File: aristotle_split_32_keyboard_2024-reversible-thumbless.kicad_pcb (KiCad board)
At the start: 2 copper layers, 100 x 87.7 mm, 43 parts, among them J1 8P8C, J2 Screw_Terminal_01x04, J3 Screw_Terminal_01x04, K13 SW_SPDT, K14 SW_SPDT, K15 SW_SPDT, K16 SW_SPDT, K17 SW_SPDT, K23 SW_SPDT, K24 SW_SPDT, K25 SW_SPDT, K26 SW_SPDT, K27 SW_SPDT, K4 SW_SPDT, K5 SW_SPDT, K6 SW_SPDT, K7 SW_SPDT, SW1 SW_SPDT, U1 ProMicro_r

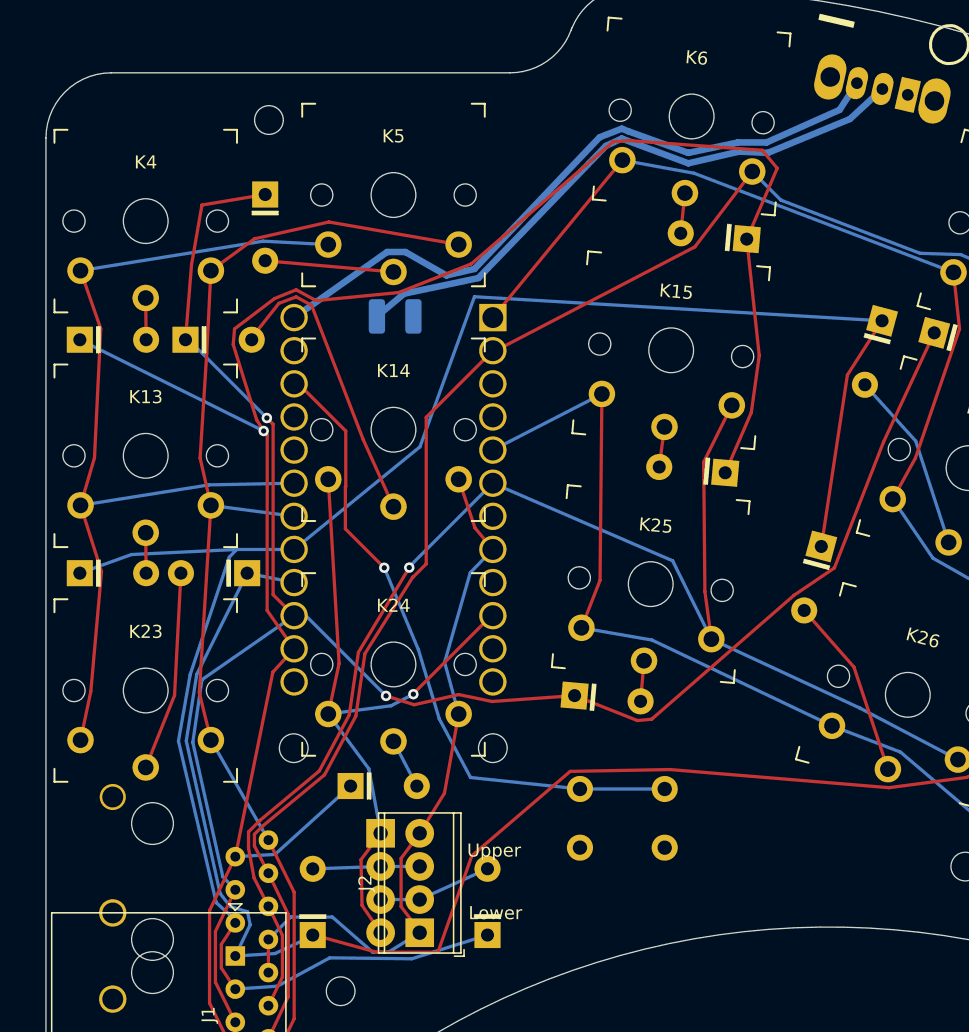
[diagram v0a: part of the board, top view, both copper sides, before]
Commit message: Move MCU up; reroute all wires to it; adjust screw positions
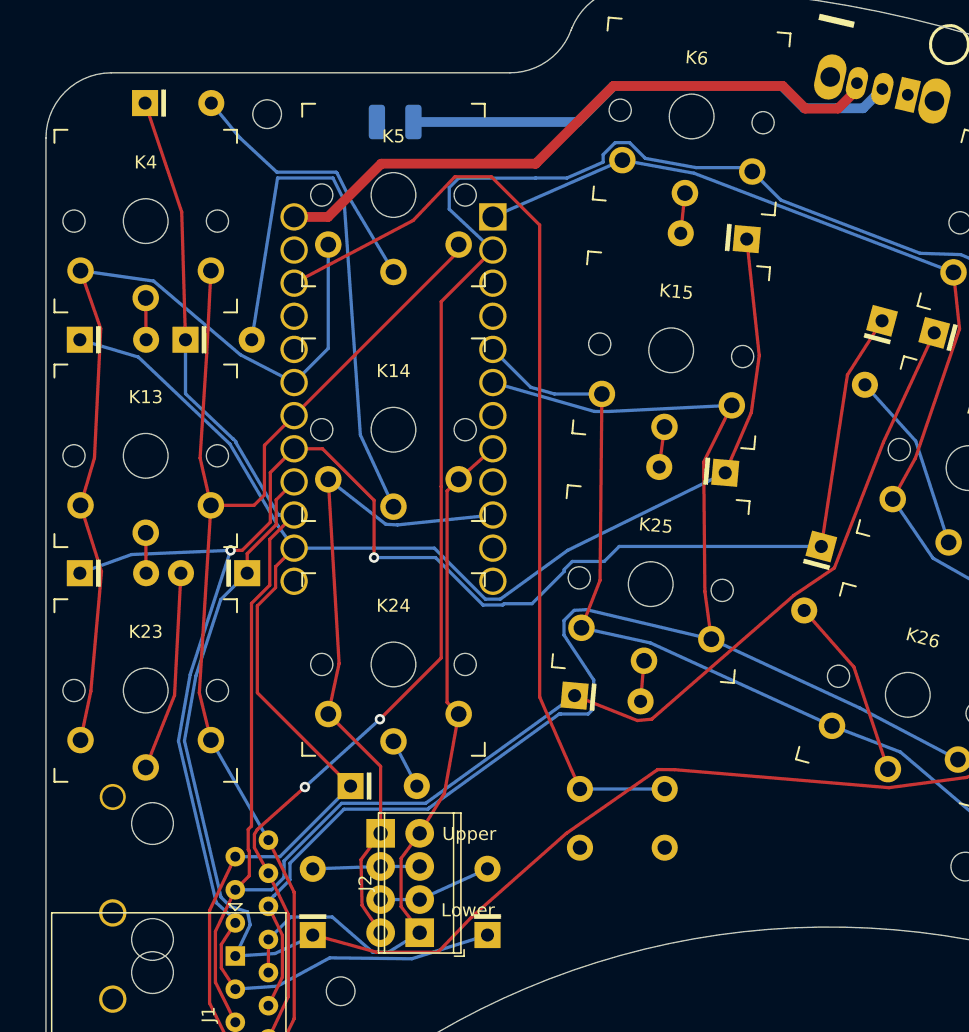
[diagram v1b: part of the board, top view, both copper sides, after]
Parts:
- removed H3: MountingHole, MountingHole:MountingHole_2.2mm_M2
- removed the H4 at (100.0, 130.4)
- moved BT1 14.9 mm to (107.8, 82.4), turned to 180 degrees
- moved D5 11.6 mm to (88.6, 81.0), turned to 0 degrees
- moved U1 7.72 mm to (107.7, 103.7)
- moved H4 0.47 mm to (98.0, 81.8)
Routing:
- net row0: track 157.0 -> 129.1 mm, vias 1 -> 0
- net Net-(U1-RST): track 49.2 -> 73.4 mm, vias 1 -> 0
- net Net-(D14-A): track 22.8 -> 42.8 mm
- net col1: track 153.7 -> 169.7 mm, vias 0 -> 2
- net Net-(D5-A): track 9.88 -> 20.7 mm
- net row1: track 143.9 -> 153.6 mm, vias 2 -> 0
- net col2: track 129.4 -> 137.6 mm, vias 1 -> 0
- net VCC: track 45.8 -> 38.4 mm
- net col7: track 72.5 -> 67.5 mm
- net col6: track 84.2 -> 79.4 mm
- net col0: track 90.3 -> 93.6 mm
- net Net-(SW1-C): track 51.8 -> 49.1 mm
- net row3: track 121.9 -> 124.6 mm
- net col3: track 54.4 -> 56.9 mm
- net row2: track 147.1 -> 146.1 mm, vias 0 -> 2
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
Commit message: Fix mounting holes
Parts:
- U1: value ProMicro_r -> Nice Nano
- renumbered H4 to H1, H4 to H2, H4 to H3
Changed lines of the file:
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@@
     (property "ki_keywords" "mounting hole")
     (attr exclude_from_pos_files)
-    (fp_text reference "H4" (at 0 -3.2) (layer "F.SilkS") hide
+    (fp_text reference "H1" (at 0 -3.2) (layer "F.SilkS") hide
         (effects (font (size 1 1) (thickness 0.15)))
     )
@@
     (property "ki_keywords" "mounting hole")
     (attr exclude_from_pos_files)
-    (fp_text reference "H4" (at 0 -3.2) (layer "F.SilkS") hide
+    (fp_text reference "H2" (at 0 -3.2) (layer "F.SilkS") hide
         (effects (font (size 1 1) (thickness 0.15)))
     )
@@
     (property "ki_keywords" "mounting hole")
     (attr exclude_from_pos_files)
-    (fp_text reference "H4" (at 0 -3.2) (layer "F.SilkS") hide
+    (fp_text reference "H3" (at 0 -3.2) (layer "F.SilkS") hide
         (effects (font (size 1 1) (thickness 0.15)))
     )
@@
         (effects (font (size 1 1) (thickness 0.15)) (justify mirror))
     )
-    (fp_text value "ProMicro_r" (at 4.07 -0.03 180) (layer "B.SilkS")
+    (fp_text value "Nice Nano" (at 5.15 -0.03 180) (layer "B.SilkS")
         (effects (font (size 1 1) (thickness 0.15)) (justify mirror))
     )
@@
     (stroke (width 0.12) (type default)) (layer "F.SilkS"))
   (gr_circle (center 97 121.5) (end 99.45 121.5)
-    (stroke (width 0.1) (type default)) (fill none) (layer "Eco1.User"))
+    (stroke (width 0.1) (type default)) (fill none) (layer "Dwgs.User"))
   (gr_circle (center 118.8 86.8) (end 121.25 86.8)
-    (stroke (width 0.1) (type default)) (fill none) (layer "Eco1.User"))
+    (stroke (width 0.1) (type default)) (fill none) (layer "Dwgs.User"))
   (gr_circle (center 96.5 86.8) (end 98.95 86.8)
-    (stroke (width 0.1) (type default)) (fill none) (layer "Eco1.User"))
+    (stroke (width 0.1) (type default)) (fill none) (layer "Dwgs.User"))
   (gr_circle (center 118.3 121.5) (end 120.75 121.5)
-    (stroke (width 0.1) (type default)) (fill none) (layer "Eco1.User"))
+    (stroke (width 0.1) (type default)) (fill none) (layer "Dwgs.User"))
   (gr_arc (start 179.010876 88.986461) (mid 180.348789 90.471737) (end 181 92.361706)
     (stroke (width 0.05) (type solid)) (layer "Edge.Cuts"))

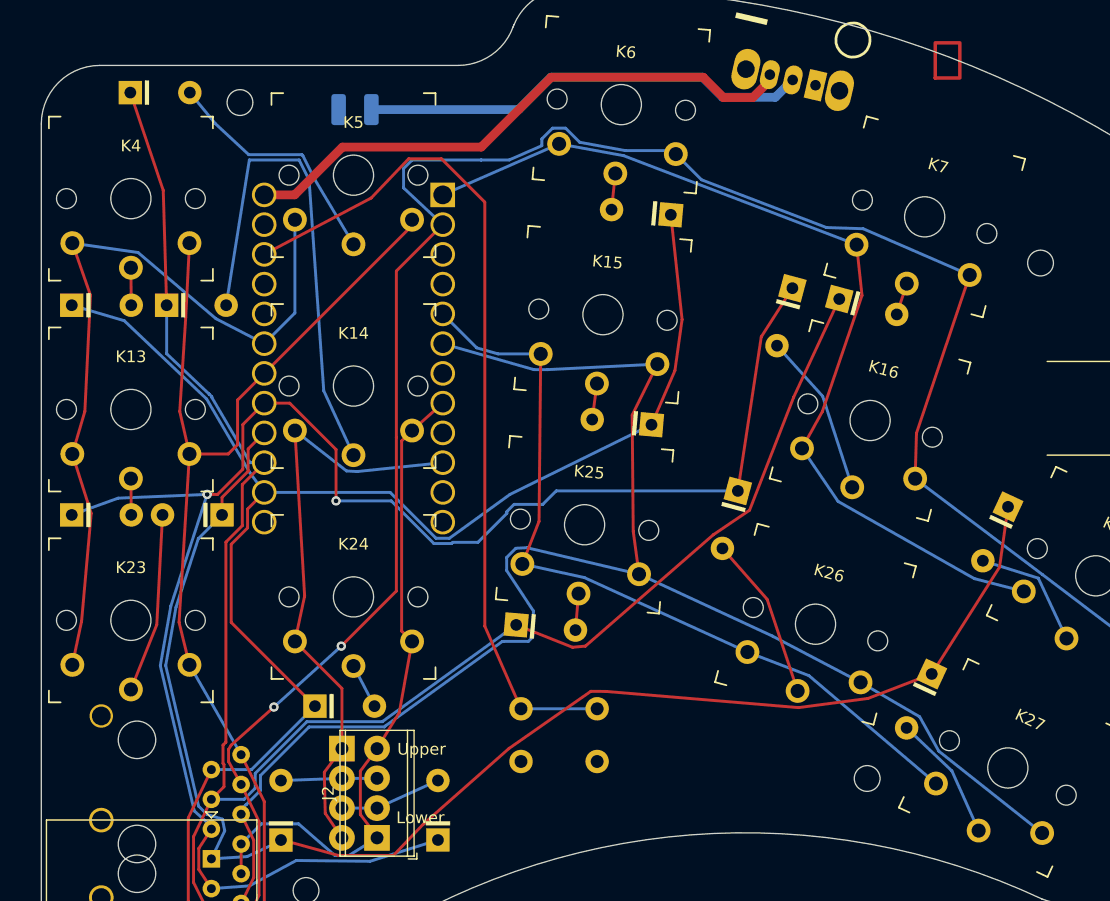
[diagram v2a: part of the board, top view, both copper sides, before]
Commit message: Adjust diode positions; move battery attachment pad
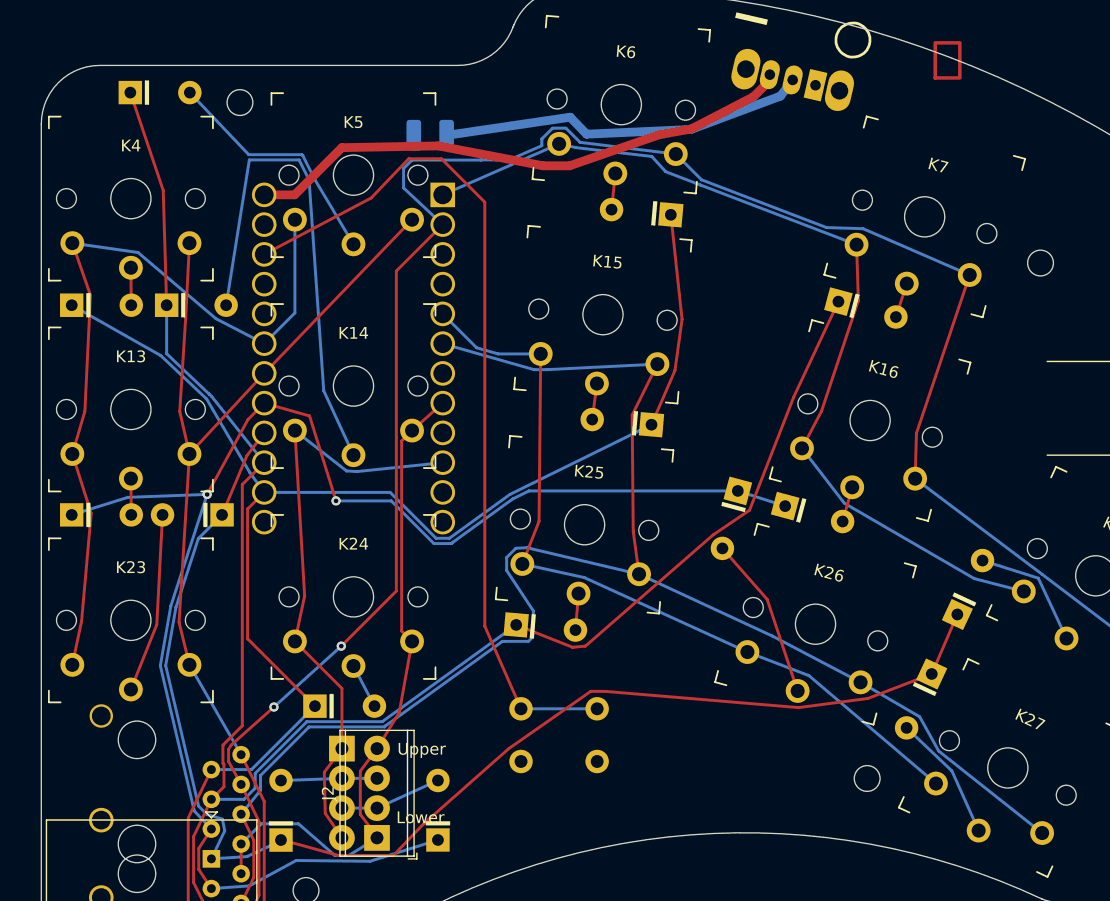
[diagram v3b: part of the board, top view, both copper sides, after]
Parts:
- U1: value Nice Nano -> NiceNano2
- moved D16 18.6 mm to (144.5, 116.2), turned to -15 degrees
- moved D17 10.2 mm to (159.2, 125.5), turned to 65 degrees
- moved BT1 6.79 mm to (114.2, 84.6)
- moved D7 0.23 mm to (149.0, 98.8)
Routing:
- net row2: track 146.1 -> 130.1 mm
- net row3: track 124.6 -> 113.5 mm
- net Net-(D16-A): track 14.0 -> 3.04 mm
- net VCC: track 38.4 -> 31.5 mm
- net Net-(SW1-C): track 49.1 -> 46.7 mm
- net col0: track 93.6 -> 91.4 mm
- net row0: track 129.1 -> 127.7 mm
- net row1: track 153.6 -> 152.9 mm
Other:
- board text added: "Bla"
- board text added: "Red"

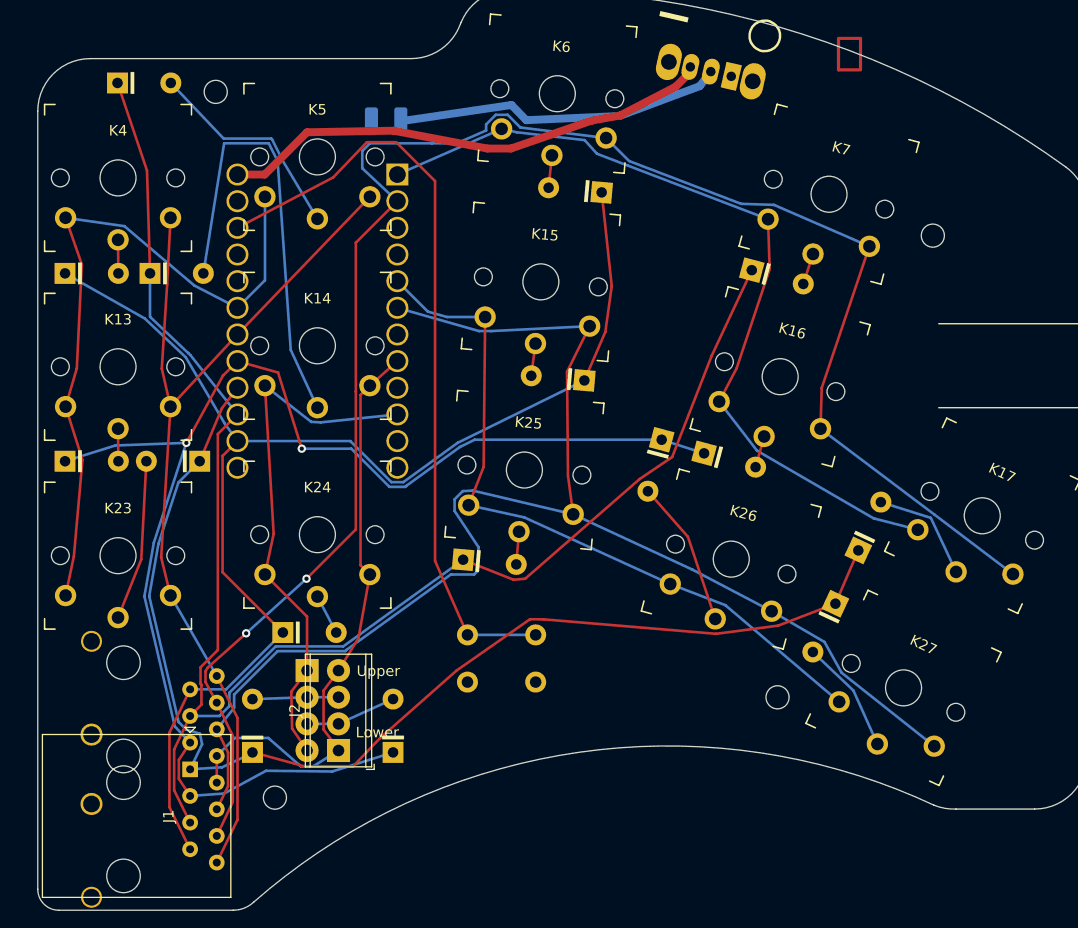
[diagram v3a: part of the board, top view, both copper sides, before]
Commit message: Reroute tracks, making default width .4 mm
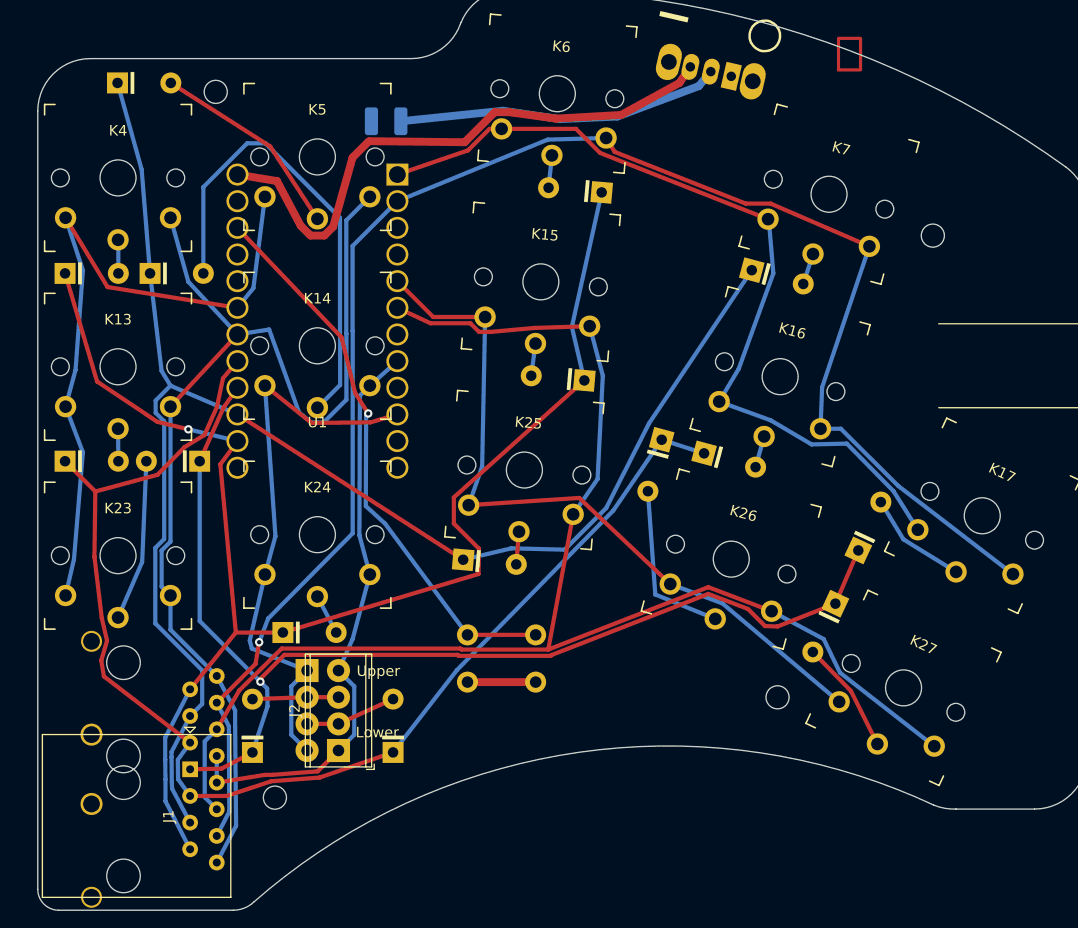
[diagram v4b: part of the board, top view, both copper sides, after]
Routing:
- net Net-(U1-RST): track 73.4 -> 53.3 mm, vias 0 -> 1
- net col0: track 91.4 -> 106.9 mm
- net col1: track 169.5 -> 158.1 mm, vias 2 -> 1
- net row2: track 130.1 -> 121.6 mm, vias 2 -> 0
- net Net-(SW1-C): track 46.7 -> 54.9 mm
- net row0: track 127.7 -> 135.0 mm, vias 0 -> 1
- net GND: track 0.00 -> 6.50 mm
- net row3: track 113.5 -> 108.9 mm, vias 0 -> 1
- net row1: track 152.9 -> 150.2 mm
- net col4: track 51.3 -> 53.9 mm
- net Net-(D14-A): track 42.8 -> 44.9 mm
- net Net-(D26-A): track 14.0 -> 16.0 mm
- net col5: track 68.4 -> 70.3 mm
- net col6: track 79.5 -> 81.0 mm
- net col3: track 56.9 -> 55.6 mm
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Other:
- board text removed: "Bla"
- board text removed: "Red"

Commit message: More rerouting
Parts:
- U1: value NiceNano2 -> ProMicro
- moved D31 19.8 mm to (98.0, 125.3), turned to -90 degrees
- moved J3 7.63 mm to (106.7, 144.6), turned to 90 degrees
- moved J2 7.62 mm to (109.7, 136.9), turned to -90 degrees
- moved D24 1.70 mm to (102.7, 133.3)
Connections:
- J2 pad 2: Net-(D30-A) -> Net-(D31-A)
- J2 pad 3: Net-(D31-A) -> Net-(D30-A)
- J3 pad 2: Net-(D31-A) -> Net-(D30-A)
- J3 pad 3: Net-(D30-A) -> Net-(D31-A)
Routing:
- net GND: track 6.50 -> 82.1 mm
- net row0: track 135.0 -> 152.9 mm
- net Net-(D31-A): track 8.20 -> 15.7 mm
- net row2: track 121.6 -> 125.4 mm
- net row3: track 108.9 -> 112.5 mm, vias 1 -> 0
- net col4: track 53.9 -> 50.8 mm
- net Net-(D14-A): track 44.9 -> 42.2 mm
- net Net-(D27-A): track 10.8 -> 12.0 mm
- net Net-(D23-A): track 15.4 -> 16.3 mm
- net col2: track 138.3 -> 137.4 mm
- net Net-(SW1-C): track 54.9 -> 55.5 mm
- net col1: track 158.1 -> 158.7 mm
- removed copper zone on B.Cu, net GND
- removed copper zone on F.Cu, net GND
